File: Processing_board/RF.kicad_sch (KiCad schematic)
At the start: 11 parts, among them IC4 BGS13SN8E6327XTSA1, IC7 CONMHF1-SMD-G-T

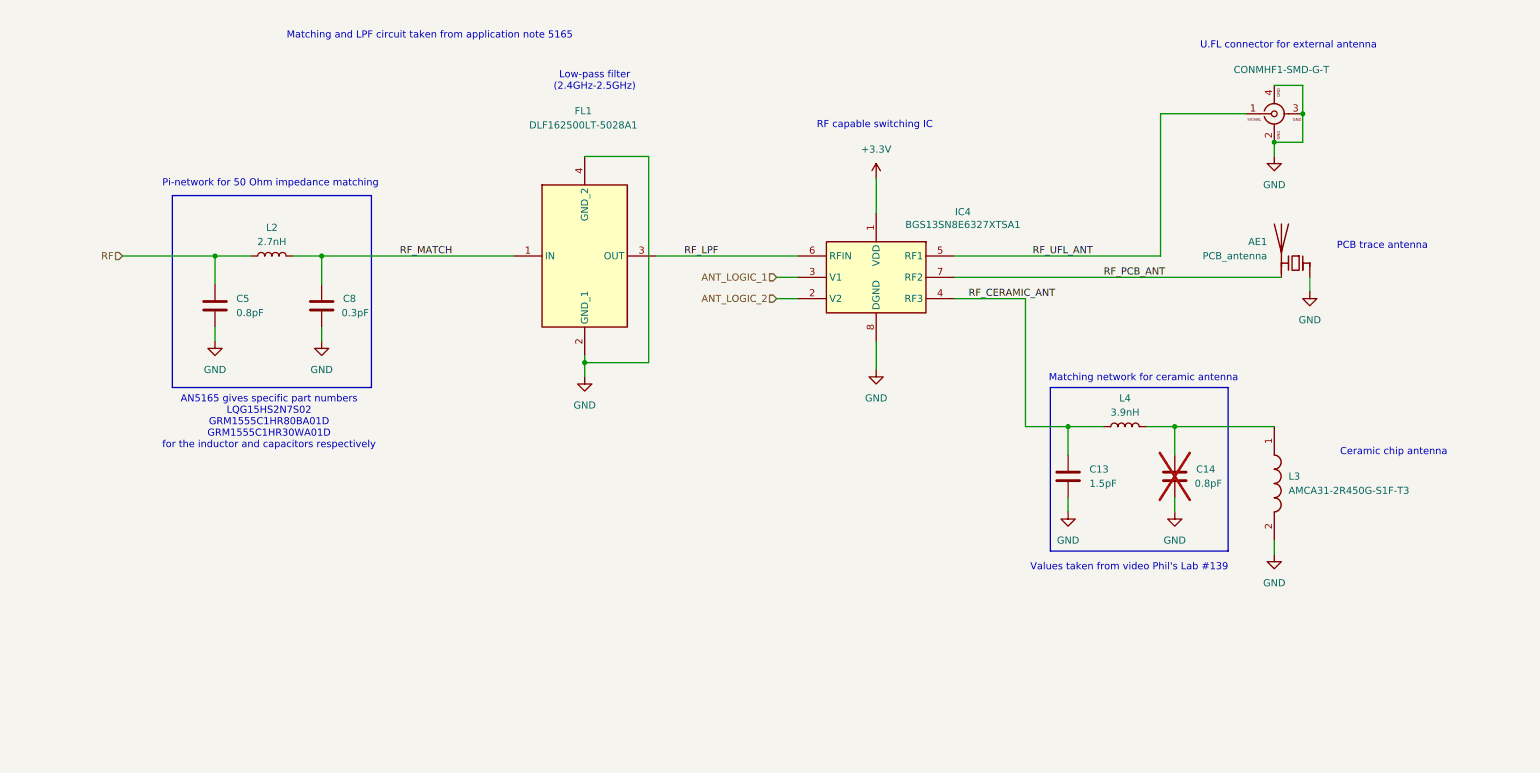
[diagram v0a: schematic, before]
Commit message: added all footprints, ready (?) to design PCB
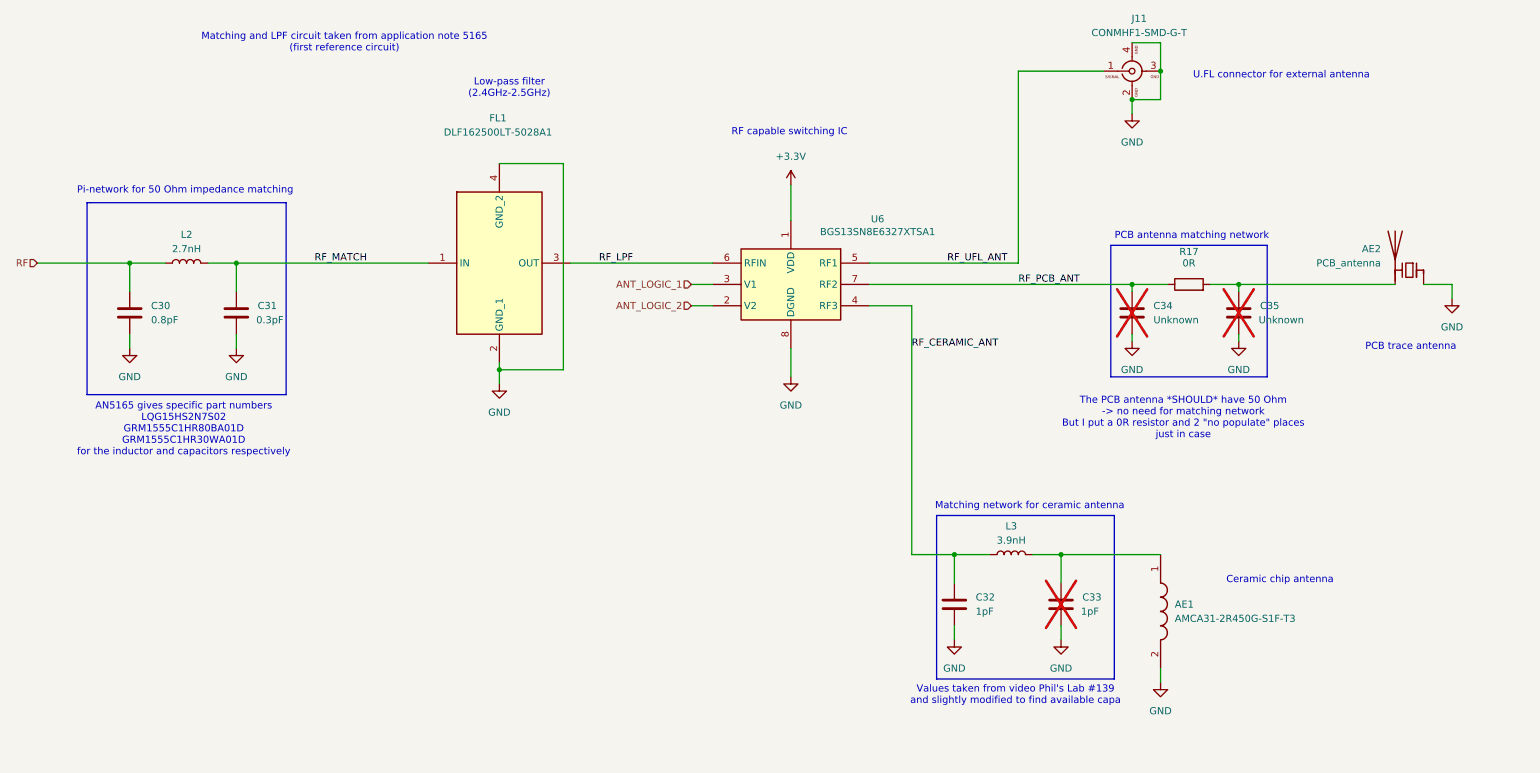
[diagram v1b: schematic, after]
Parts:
- added C34, C35: Unknown, Capacitor_SMD:C_0402_1005Metric, symbol Device:C
- added R17: 0R, Resistor_SMD:R_01005_0402Metric, symbol Device:R
- AE1: renamed from L3; footprint ANTC3216X140N -> AMCA31-2R450G-S1F-T3:ANTC3216X140N
- AE2: renamed from AE1; footprint (none) -> RF_Antenna:Texas_SWRA117D_2.4GHz_Right
- C30: renamed from C5; footprint (none) -> Capacitor_SMD:C_0402_1005Metric
- C31: renamed from C8; footprint (none) -> Capacitor_SMD:C_0402_1005Metric
- C32: renamed from C13; value 1.5pF -> 1pF; footprint (none) -> Capacitor_SMD:C_0603_1608Metric
- C33: renamed from C14; value 0.8pF -> 1pF; footprint (none) -> Capacitor_SMD:C_0603_1608Metric
- FL1: footprint DLF162500LT5028A1 -> DLF162500LT-5028A1:DLF162500LT5028A1
- J11: renamed from IC7; footprint CONMHF1SMDGT -> CONMHF1-SMD-G-T:CONMHF1SMDGT
- L2: footprint (none) -> Inductor_SMD:L_0402_1005Metric
- L3: renamed from L4; footprint (none) -> Inductor_SMD:L_0402_1005Metric
- U6: renamed from IC4; footprint BGS13SN8E6327XTSA1 -> BGS13SN8E6327XTSA1:BGS13SN8E6327XTSA1
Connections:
- net GND: now also C34.2, C35.2
- net RF_PCB_ANT: now also C34.1, R17.1; no longer AE2.2 (PCB_Trace)
- new net: AE2.2 (PCB_Trace), C35.1, R17.2
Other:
- note added: "Matching and LPF circuit taken from application note 5165 (first reference circuit)"
- note added: "PCB antenna matching network"
- note added: "The PCB antenna *SHOULD* have 50 Ohm -> no need for matching network But I put a 0R resistor and 2 "no populate" places just in case"
- note added: "Values taken from video Phil's Lab #139 and slightly modified to find available capa"
- note removed: "Matching and LPF circuit taken from application note 5165"
- note removed: "Values taken from video Phil's Lab #139"
- moved on the sheet: AE1, AE2, C30, C31, C32, C33, FL1, L2, L3, U6

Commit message: first draft of PCB almost done
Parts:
- AE2: footprint RF_Antenna:Texas_SWRA117D_2.4GHz_Right -> RF_Antenna:Texas_SWRA117D_2.4GHz_Left
- C30: renamed from C32; value 1pF -> 1.5pF; footprint Capacitor_SMD:C_0603_1608Metric -> Capacitor_SMD:C_0402_1005Metric
- C31: renamed from C33; value 1pF -> 1.5pF; footprint Capacitor_SMD:C_0603_1608Metric -> Capacitor_SMD:C_0402_1005Metric
- R17: footprint Resistor_SMD:R_01005_0402Metric -> Resistor_SMD:R_0402_1005Metric
- renumbered C30 to C28, C31 to C29, C34 to C32, C35 to C33
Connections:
- net RF_CERAMIC_ANT: now also AE1.1 (FEED), C31.1, L3.2; no longer C30.1, L3.1, U6.4 (RF3)
- net RF_PCB_ANT: now also AE2.2 (PCB_Trace), C33.1, R17.2; no longer C32.1, R17.1, U6.7 (RF2)
- new net RF_CERAMIC_MATCH: C30.1, L3.1, U6.7 (RF2)
- new net RF_PCB_MATCH: C32.1, R17.1, U6.4 (RF3)
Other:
- note added: "Values taken from antenna datasheet and Phil's lab #139 but slightly modified (1.5pF->1pF) to find available capa"
- note removed: "Values taken from video Phil's Lab #139 and slightly modified to find available capa"
- moved on the sheet: AE1, AE2, C30, C31, C32, C33, L3, R17

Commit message: ELEA V1
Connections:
- net GND: now also AE2.2 (PCB_Trace); no longer AE2.1 (FEED)
- net RF_PCB_ANT: now also AE2.1 (FEED); no longer AE2.2 (PCB_Trace)
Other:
- moved on the sheet: AE2
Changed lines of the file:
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@@
+	(wire
+		(pts
+			(xy 224.79 120.65) (xy 229.87 120.65)
+		)
+		(stroke
+			(width 0)
+			(type default)
+		)
+	)
 	(wire
 		(pts
@@
 	(wire
 		(pts
+			(xy 194.31 25.4) (xy 209.55 25.4)
+		)
+		(stroke
+			(width 0)
+			(type default)
+		)
+	)
+	(wire
+		(pts
 			(xy 191.77 120.65) (xy 219.71 120.65)
-		)
-		(stroke
-			(width 0)
-			(type default)
-		)
-	)
-	(wire
-		(pts
-			(xy 194.31 25.4) (xy 209.55 25.4)
-		)
-		(stroke
-			(width 0)
-			(type default)
-		)
-	)
-	(wire
-		(pts
-			(xy 224.79 120.65) (xy 229.87 120.65)
 		)
 		(stroke
@@
 		(lib_id "Device:Antenna_Chip")
 		(at 222.25 118.11 0)
-		(mirror y)
 		(unit 1)
 		(exclude_from_sim no)
@@
 		(dnp no)
 		(property "Reference" "AE2"
-			(at 217.17 114.2999 0)
+			(at 227.33 114.2999 0)
 			(effects
 				(font
@@
 		)
 		(property "Value" "PCB_antenna"
-			(at 217.17 116.8399 0)
+			(at 227.33 116.8399 0)
 			(effects
 				(font
@@
 		)
 		(property "Footprint" "RF_Antenna:Texas_SWRA117D_2.4GHz_Left"
-			(at 224.79 113.665 0)
+			(at 219.71 113.665 0)
 			(effects
 				(font
@@
 		)
 		(property "Datasheet" "~"
-			(at 224.79 113.665 0)
-			(effects
-				(font
+			(at 219.71 113.665 0)
+			(effects
+				(font

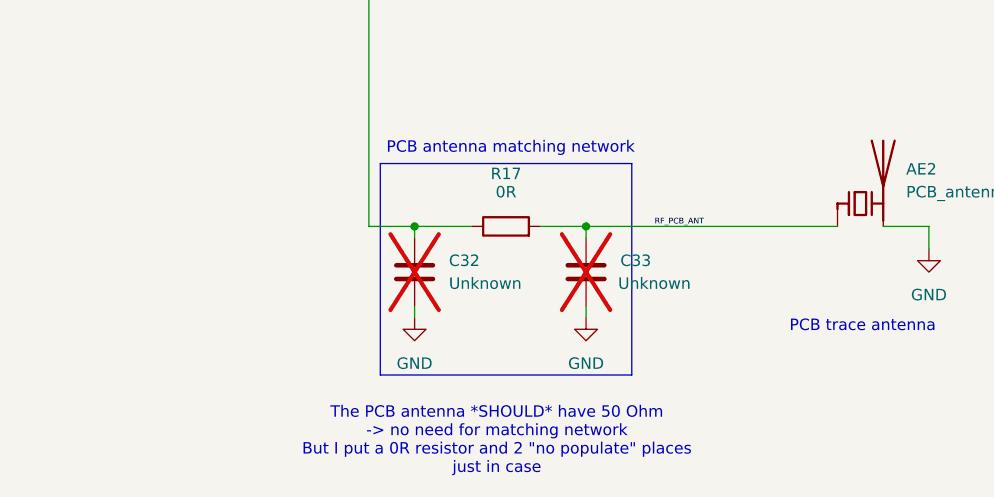
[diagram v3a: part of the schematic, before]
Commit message: changed antenna placement and added GND pour on layer1 and 4
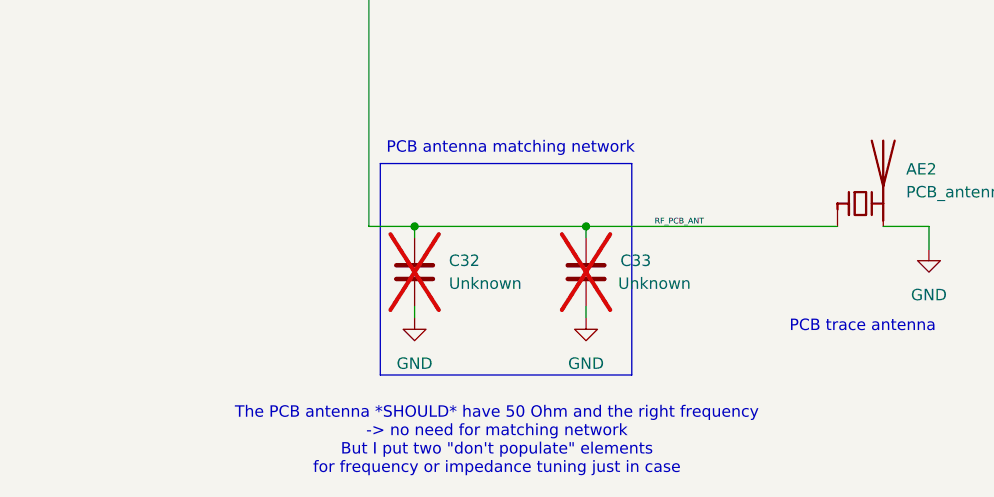
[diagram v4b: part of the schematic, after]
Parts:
- removed R17: 0R, Resistor_SMD:R_0402_1005Metric, symbol Device:R
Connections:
- net RF_PCB_MATCH is gone; now on net RF_PCB_ANT: C32.1, U6.4 (RF3)
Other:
- note added: "The PCB antenna *SHOULD* have 50 Ohm and the right frequency -> no need for matching network But I put two "don't populate" elements for frequency or impedance tuning just in case"
- note removed: "The PCB antenna *SHOULD* have 50 Ohm -> no need for matching network But I put a 0R resistor and 2 "no populate" places just in case"
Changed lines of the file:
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@@
 		(company "N-Pulse")
 	)
-	(text "The PCB antenna *SHOULD* have 50 Ohm \n-> no need for matching network\nBut I put a 0R resistor and 2 \"no populate\" places\njust in case"
+	(text "The PCB antenna *SHOULD* have 50 Ohm and the right frequency\n-> no need for matching network\nBut I put two \"don't populate\" elements \nfor frequency or impedance tuning just in case"
 		(exclude_from_sim no)
 		(at 181.864 144.526 0)
@@
 	)
 	(junction
+		(at 172.72 120.65)
+		(diameter 0)
+		(color 0 0 0 0)
+	)
+	(junction
 		(at 54.61 59.69)
 		(diameter 0)
@@
 	)
 	(junction
-		(at 172.72 120.65)
-		(diameter 0)
-		(color 0 0 0 0)
-	)
-	(junction
 		(at 214.63 30.48)
 		(diameter 0)
@@
 	(wire
 		(pts
-			(xy 167.64 120.65) (xy 172.72 120.65)
+			(xy 172.72 120.65) (xy 191.77 120.65)
 		)
 		(stroke
@@
 	(wire
 		(pts
-			(xy 172.72 120.65) (xy 179.07 120.65)
+			(xy 172.72 120.65) (xy 167.64 120.65)
 		)
 		(stroke
@@
 		(pts
 			(xy 113.03 78.74) (xy 101.6 78.74)
-		)
-		(stroke
-			(width 0)
-			(type default)
-		)
-	)
-	(wire
-		(pts
-			(xy 186.69 120.65) (xy 191.77 120.65)
 		)
 		(stroke
@@
 					(unit 1)
 				)
-			)
-		)
-	)
-	(symbol
-		(lib_id "Device:R")
-		(at 182.88 120.65 90)
-		(unit 1)
-		(exclude_from_sim no)
-		(in_bom yes)
-		(on_board yes)
-		(dnp no)
-		(property "Reference" "R17"
-			(at 182.88 114.808 90)
-			(effects
-				(font
-					(size 1.27 1.27)
-				)
-			)
-		)
-		(property "Value" "0R"
-			(at 182.88 116.84 90)
-			(effects
-				(font
-					(size 1.27 1.27)
-				)
-			)
-		)
-		(property "Footprint" "Resistor_SMD:R_0402_1005Metric"
-			(at 182.88 122.428 90)
-			(effects
-				(font
-					(size 1.27 1.27)
-				)
-				(hide yes)
-			)
-		)
-		(property "Datasheet" "~"
-			(at 182.88 120.65 0)
-			(effects
-				(font
-					(size 1.27 1.27)
-				)
-				(hide yes)
-			)
-		)
-		(property "Description" "Resistor"
-			(at 182.88 120.65 0)
-			(effects
-				(font
-					(size 1.27 1.27)
-				)
-				(hide yes)
-			)
-		)
-		(pin "2"
-		)
-		(pin "1"
-		)
-		(instances
-			(project ""
-				(path "/b48cfd4a-6c36-4270-b2b4-45cb26e35477/d5efe196-3030-4740-bb6d-2e5f674a846e"
-					(reference "R17")
-					(unit 1)
-				)

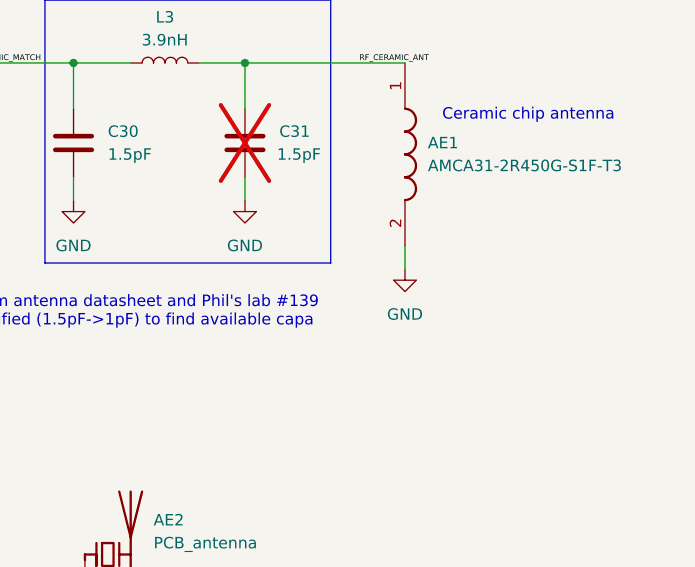
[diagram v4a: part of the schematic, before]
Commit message: minor changes to correct DRC warnings
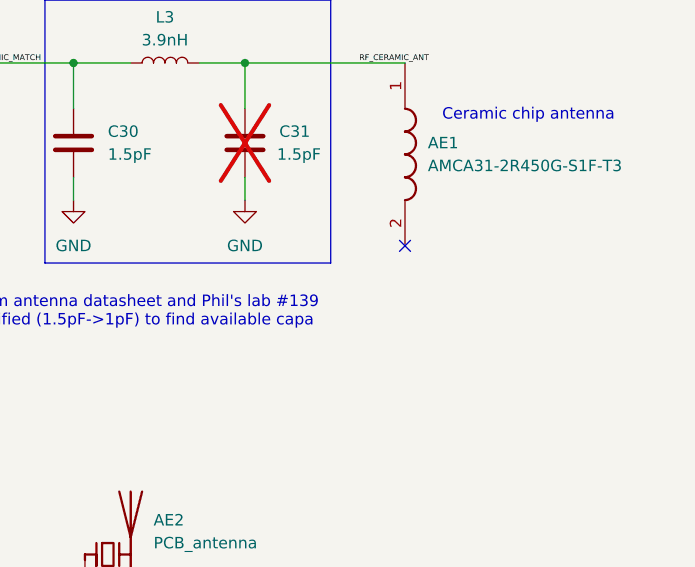
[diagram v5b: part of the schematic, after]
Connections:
- net GND: no longer AE1.2 (NC)
- no-connect marks 0 -> 1
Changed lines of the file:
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@@
 		(color 0 0 0 0)
 	)
+	(no_connect
+		(at 255.27 83.82)
+	)
 	(wire
 		(pts
@@
 		(pts
 			(xy 54.61 72.39) (xy 54.61 74.93)
-		)
-		(stroke
-			(width 0)
-			(type default)
-		)
-	)
-	(wire
-		(pts
-			(xy 255.27 83.82) (xy 255.27 86.36)
 		)
 		(stroke
@@
 					(unit 1)
 				)
-			)
-		)
-	)
-	(symbol
-		(lib_id "power:GND")
-		(at 255.27 86.36 0)
-		(unit 1)
-		(exclude_from_sim no)
-		(in_bom yes)
-		(on_board yes)
-		(dnp no)
-		(fields_autoplaced yes)
-		(property "Reference" "#PWR045"
-			(at 255.27 92.71 0)
-			(effects
-				(font
-					(size 1.27 1.27)
-				)
-				(hide yes)
-			)
-		)
-		(property "Value" "GND"
-			(at 255.27 91.44 0)
-			(effects
-				(font
-					(size 1.27 1.27)
-				)
-			)
-		)
-		(property "Footprint" ""
-			(at 255.27 86.36 0)
-			(effects
-				(font
-					(size 1.27 1.27)
-				)
-				(hide yes)
-			)
-		)
-		(property "Datasheet" ""
-			(at 255.27 86.36 0)
-			(effects
-				(font
-					(size 1.27 1.27)
-				)
-				(hide yes)
-			)
-		)
-		(property "Description" "Power symbol creates a global label with name \"GND\" , ground"
-			(at 255.27 86.36 0)
-			(effects
-				(font
-					(size 1.27 1.27)
-				)
-				(hide yes)
-			)
-		)
-		(pin "1"
-		)
-		(instances
-			(project ""
-				(path "/b48cfd4a-6c36-4270-b2b4-45cb26e35477/d5efe196-3030-4740-bb6d-2e5f674a846e"
-					(reference "#PWR045")
-					(unit 1)
-				)

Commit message: more minor cleanup
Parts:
- renumbered AE2 to AE1, AE1 to AE2, C32 to C30, C33 to C31, C30 to C32, C31 to C33
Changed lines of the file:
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@@
 		(dnp no)
 		(fields_autoplaced yes)
-		(property "Reference" "#PWR036"
+		(property "Reference" "#PWR039"
 			(at 35.56 81.28 0)
 			(effects
@@
 			(project ""
 				(path "/b48cfd4a-6c36-4270-b2b4-45cb26e35477/d5efe196-3030-4740-bb6d-2e5f674a846e"
-					(reference "#PWR036")
+					(reference "#PWR039")
 					(unit 1)
 				)
@@
 		(dnp no)
 		(fields_autoplaced yes)
-		(property "Reference" "#PWR037"
+		(property "Reference" "#PWR040"
 			(at 54.61 81.28 0)
 			(effects
@@
 			(project ""
 				(path "/b48cfd4a-6c36-4270-b2b4-45cb26e35477/d5efe196-3030-4740-bb6d-2e5f674a846e"
-					(reference "#PWR037")
+					(reference "#PWR040")
 					(unit 1)
 				)
@@
 		(on_board yes)
 		(dnp no)
-		(property "Reference" "AE2"
+		(property "Reference" "AE1"
 			(at 227.33 114.2999 0)
 			(effects
@@
 			(project ""
 				(path "/b48cfd4a-6c36-4270-b2b4-45cb26e35477/d5efe196-3030-4740-bb6d-2e5f674a846e"
-					(reference "AE2")
+					(reference "AE1")
 					(unit 1)
 				)
@@
 		(dnp no)
 		(fields_autoplaced yes)
-		(property "Reference" "#PWR046"
+		(property "Reference" "#PWR045"
 			(at 191.77 137.16 0)
 			(effects
@@
 			(project "Processing_board"
 				(path "/b48cfd4a-6c36-4270-b2b4-45cb26e35477/d5efe196-3030-4740-bb6d-2e5f674a846e"
-					(reference "#PWR046")
+					(reference "#PWR045")
 					(unit 1)
 				)
@@
 		(dnp no)
 		(fields_autoplaced yes)
-		(property "Reference" "#PWR041"
+		(property "Reference" "#PWR047"
 			(at 218.44 85.09 0)
 			(effects
@@
 			(project "Processing_board"
 				(path "/b48cfd4a-6c36-4270-b2b4-45cb26e35477/d5efe196-3030-4740-bb6d-2e5f674a846e"
-					(reference "#PWR041")
+					(reference "#PWR047")
 					(unit 1)
 				)
@@
 		(dnp no)
 		(fields_autoplaced yes)
-		(property "Reference" "#PWR038"
+		(property "Reference" "#PWR041"
 			(at 101.6 87.63 0)
 			(effects
@@
 			(project "Processing_board"
 				(path "/b48cfd4a-6c36-4270-b2b4-45cb26e35477/d5efe196-3030-4740-bb6d-2e5f674a846e"
-					(reference "#PWR038")
+					(reference "#PWR041")
 					(unit 1)
 				)
@@
 		(dnp no)
 		(fields_autoplaced yes)
-		(property "Reference" "#PWR039"
+		(property "Reference" "#PWR042"
 			(at 153.67 49.53 0)
 			(effects
@@
 			(project ""
 				(path "/b48cfd4a-6c36-4270-b2b4-45cb26e35477/d5efe196-3030-4740-bb6d-2e5f674a846e"
-					(reference "#PWR039")
+					(reference "#PWR042")
 					(unit 1)
 				)
@@
 		(dnp no)
 		(fields_autoplaced yes)
-		(property "Reference" "#PWR043"
+		(property "Reference" "#PWR046"
 			(at 214.63 39.37 0)
 			(effects
@@
 			(project "Processing_board"
 				(path "/b48cfd4a-6c36-4270-b2b4-45cb26e35477/d5efe196-3030-4740-bb6d-2e5f674a846e"
-					(reference "#PWR043")
+					(reference "#PWR046")
 					(unit 1)
 				)
@@
 		(dnp yes)
 		(fields_autoplaced yes)
-		(property "Reference" "C32"
+		(property "Reference" "C30"
 			(at 176.53 124.4599 0)
 			(effects
@@
 			(project "Processing_board"
 				(path "/b48cfd4a-6c36-4270-b2b4-45cb26e35477/d5efe196-3030-4740-bb6d-2e5f674a846e"
-					(reference "C32")
+					(reference "C30")
 					(unit 1)
 				)
@@
 		(dnp no)
 		(fields_autoplaced yes)
-		(property "Reference" "AE1"
+		(property "Reference" "AE2"
 			(at 257.81 72.3899 90)
 			(effects
@@
 			(project ""
 				(path "/b48cfd4a-6c36-4270-b2b4-45cb26e35477/d5efe196-3030-4740-bb6d-2e5f674a846e"
-					(reference "AE1")
+					(reference "AE2")
 					(unit 1)
 				)
@@
 		(dnp no)
 		(fields_autoplaced yes)
-		(property "Reference" "#PWR042"
+		(property "Reference" "#PWR049"
 			(at 237.49 85.09 0)
 			(effects
@@
 			(project "Processing_board"
 				(path "/b48cfd4a-6c36-4270-b2b4-45cb26e35477/d5efe196-3030-4740-bb6d-2e5f674a846e"
-					(reference "#PWR042")
+					(reference "#PWR049")
 					(unit 1)
 				)
@@
 		(dnp no)
 		(fields_autoplaced yes)
-		(property "Reference" "#PWR047"
+		(property "Reference" "#PWR048"
 			(at 229.87 129.54 0)
 			(effects
@@
 			(project ""
 				(path "/b48cfd4a-6c36-4270-b2b4-45cb26e35477/d5efe196-3030-4740-bb6d-2e5f674a846e"
-					(reference "#PWR047")
+					(reference "#PWR048")
 					(unit 1)
 				)
@@
 		(on_board yes)
 		(dnp yes)
-		(property "Reference" "C33"
+		(property "Reference" "C31"
 			(at 195.58 124.4599 0)
 			(effects
@@
 			(project "Processing_board"
 				(path "/b48cfd4a-6c36-4270-b2b4-45cb26e35477/d5efe196-3030-4740-bb6d-2e5f674a846e"
-					(reference "C33")
+					(reference "C31")
 					(unit 1)
 				)
@@
 		(dnp no)
 		(fields_autoplaced yes)
-		(property "Reference" "#PWR040"
+		(property "Reference" "#PWR043"
 			(at 153.67 86.36 0)
 			(effects
@@
 			(project ""
 				(path "/b48cfd4a-6c36-4270-b2b4-45cb26e35477/d5efe196-3030-4740-bb6d-2e5f674a846e"
-					(reference "#PWR040")
+					(reference "#PWR043")
 					(unit 1)
 				)
@@
 		(dnp no)
 		(fields_autoplaced yes)
-		(property "Reference" "C30"
+		(property "Reference" "C32"
 			(at 222.25 71.1199 0)
 			(effects
@@
 			(project "Processing_board"
 				(path "/b48cfd4a-6c36-4270-b2b4-45cb26e35477/d5efe196-3030-4740-bb6d-2e5f674a846e"
-					(reference "C30")
+					(reference "C32")
 					(unit 1)
 				)
@@
 		(on_board yes)
 		(dnp yes)
-		(property "Reference" "C31"
+		(property "Reference" "C33"
 			(at 241.3 71.1199 0)
 			(effects
@@
 			(project "Processing_board"
 				(path "/b48cfd4a-6c36-4270-b2b4-45cb26e35477/d5efe196-3030-4740-bb6d-2e5f674a846e"
-					(reference "C31")
-					(unit 1)
-				)
+					(reference "C33")
+					(unit 1)
+				)

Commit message: more cleanup
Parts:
- renumbered AE1 to AE3, AE2 to AE4, C32 to C102, C33 to C105, C28 to C57, C29 to C61, C30 to C91, C31 to C94, FL1 to FL2, J11 to J22, L2 to L4, L3 to L6, U6 to U15
